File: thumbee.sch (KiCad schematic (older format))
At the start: 65 parts, among them J11 Conn_02x05_Odd_Even, J12 USB_B, U1 msc313e, U2 spinor, U3 ht42b534-1, U4 RT8059GJ5, U5 RT8059GJ5, U6 RT8059GJ5, U7 xc6204xxxxMR, Y1 Crystal

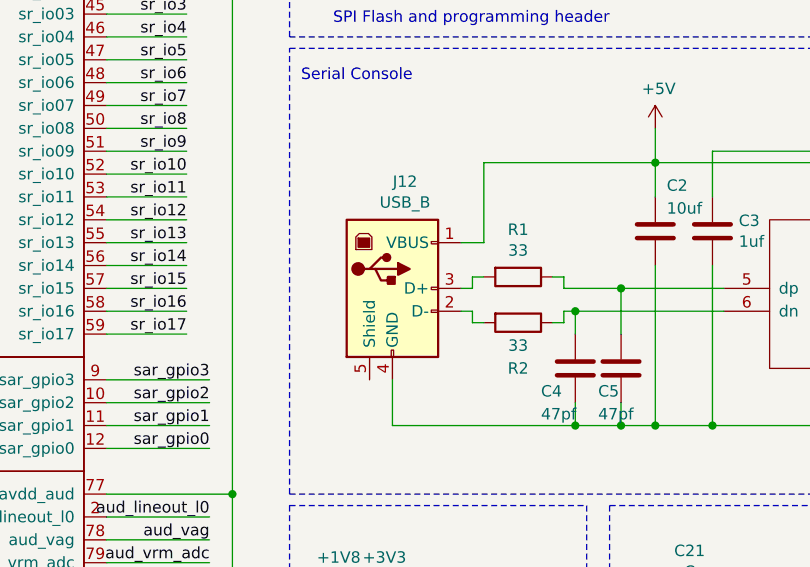
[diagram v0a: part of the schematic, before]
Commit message: Fix USB pinout
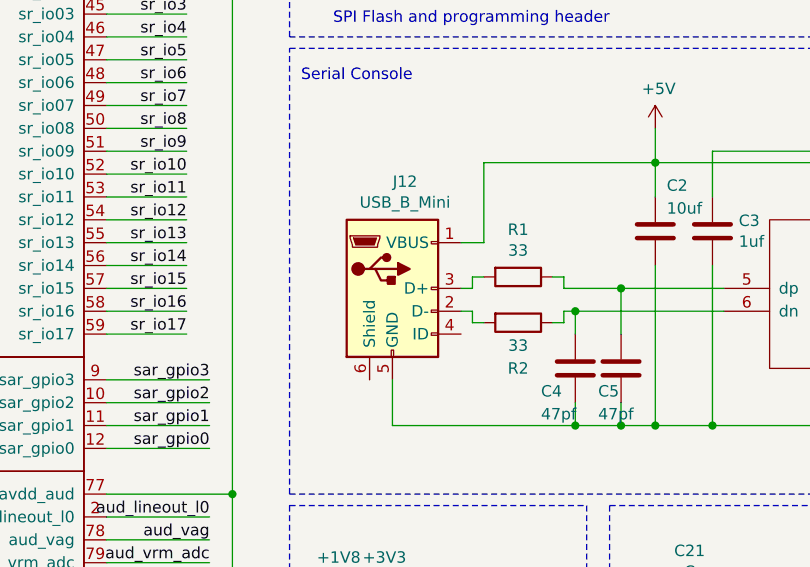
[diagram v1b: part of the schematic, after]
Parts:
- removed J12: USB_B, USB-MICRO-MK5P-2:USB-MICRO-B, symbol Connector:USB_B
- added J12: USB_B_Mini, USB-MICRO-MK5P-2:USB-MICRO-B, symbol Connector:USB_B_Mini
- U1: footprint (none) -> s2qfn80:QFN-80_EP_8x8_Pitch0.35mm
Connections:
- net +5V: now also J12.1 (VBUS)
- net GND: now also J12.5 (GND)
- net at R2.2: now also J12.2 (D-)
- net at R1.2: now also J12.3 (D+)
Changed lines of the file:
@@
 F 0 "U1" H 2950 1300 50  0000 C CNN
 F 1 "msc313e" H 2950 1200 50  0000 C CNN
-F 2 "" H 1200 5450 50  0001 C CNN
+F 2 "s2qfn80:QFN-80_EP_8x8_Pitch0.35mm" H 1200 5450 50  0001 C CNN
 F 3 "" H 1200 5450 50  0001 C CNN
 	1    2400 3800
@@
 Text Notes 8200 5650 2    50   ~ 0
 Reset
-$Comp
-L Connector:USB_B J12
-U 1 1 5C6DEC42
-P 4800 3350
-F 0 "J12" H 4855 3817 50  0000 C CNN
-F 1 "USB_B" H 4855 3726 50  0000 C CNN
-F 2 "USB-MICRO-MK5P-2:USB-MICRO-B" H 4950 3300 50  0001 C CNN
-F 3 " ~" H 4950 3300 50  0001 C CNN
-	1    4800 3350
-	1    0    0    -1
-$EndComp
 $Comp
 L Device:R R1
@@
 	1    0    0    -1
 $EndComp
+$Comp
+L Connector:USB_B_Mini J12
+U 1 1 5C8EB53D
+P 4800 3350
+F 0 "J12" H 4855 3817 50  0000 C CNN
+F 1 "USB_B_Mini" H 4855 3726 50  0000 C CNN
+F 2 "USB-MICRO-MK5P-2:USB-MICRO-B" H 4950 3300 50  0001 C CNN
+F 3 "~" H 4950 3300 50  0001 C CNN
+	1    4800 3350
+	1    0    0    -1
+$EndComp
